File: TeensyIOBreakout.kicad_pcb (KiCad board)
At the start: 2 copper layers, 26 parts, among them J1 Conn_01x02_Male, J10 Conn_01x02_Male, J11 Conn_01x02_Male, J12 Conn_01x02_Male, J13 Conn_01x02_Male, J14 Conn_01x02_Male, J15 Conn_01x02_Male, J16 Conn_01x02_Male, J17 Conn_01x02_Male, J18 Conn_01x02_Male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

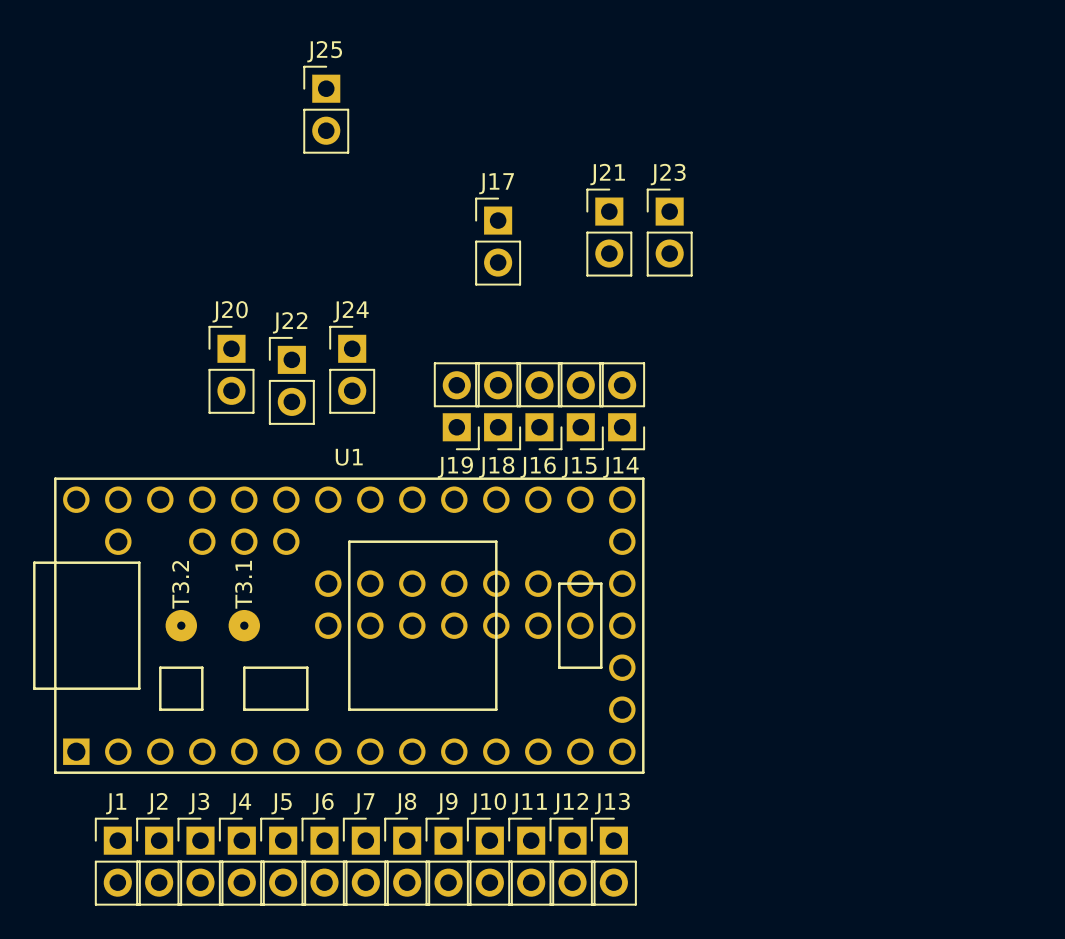
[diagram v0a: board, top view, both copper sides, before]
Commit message: Updated SCH and PCB to use fewer header footprints
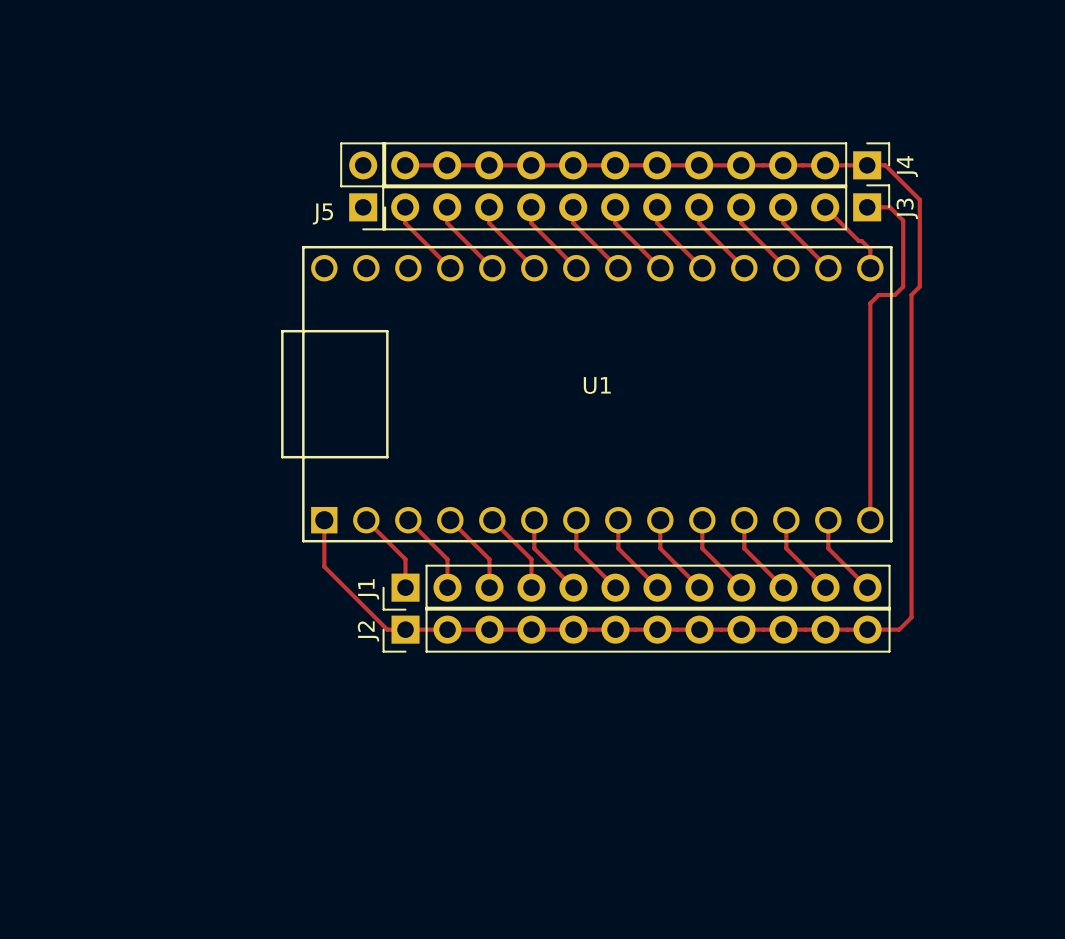
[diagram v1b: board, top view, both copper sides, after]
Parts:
- removed J10, J11, J12, J13, J14, J15, J16, J17, J18, J19, J20, J21, J22, J23, J24, J25, J6, J7, J8, J9: Conn_01x02_Male, Pin_Headers:Pin_Header_Straight_1x02_Pitch2.54mm
- J1, J2, J3, J4: value Conn_01x02_Male -> Conn_01x12_Male; footprint Pin_Headers:Pin_Header_Straight_1x02_Pitch2.54mm -> Pin_Headers:Pin_Header_Straight_1x12_Pitch2.54mm
- U1: footprint teensy:Teensy30_31_32_LC -> Teensy32NoCenterPads:Teensy30_31_32_LC_NoCenterPads
- moved J4 55.7 mm to (146.3, 24.7), turned to 270 degrees
- moved J3 55.6 mm to (146.3, 27.2), turned to 270 degrees
- moved J5 38.6 mm to (115.8, 27.2), turned to 180 degrees
- moved J1 23.2 mm to (118.4, 50.2), turned to 90 degrees
- moved U1 20.5 mm to (130.0, 38.5)
- moved J2 19.6 mm to (118.4, 52.7), turned to 90 degrees
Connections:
- J1 pad 2: GND -> IO_1
- J2 pad 1: IO_1 -> GND
- J3 pad 1: IO_2 -> IO_12
- J3 pad 2: GND -> IO_13
- J4 pad 1: IO_3 -> GND
- J5 pad 1: IO_4 -> Vin
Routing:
- net GND: track 0.00 -> 97.7 mm
- net IO_12: track 0.00 -> 22.0 mm
- net IO_9: track 0.00 -> 5.06 mm
- net IO_8: track 0.00 -> 5.06 mm
- net IO_7: track 0.00 -> 5.06 mm
- net IO_5: track 0.00 -> 5.06 mm
- net IO_4: track 0.00 -> 5.06 mm
- net IO_2: track 0.00 -> 5.06 mm
- net IO_11: track 0.00 -> 5.06 mm
- net IO_10: track 0.00 -> 5.06 mm
- net IO_1: track 0.00 -> 5.06 mm
- net IO_0: track 0.00 -> 5.06 mm
- net IO_3: track 0.00 -> 5.06 mm
- net IO_6: track 0.00 -> 5.06 mm
- net IO_13: track 0.00 -> 4.92 mm
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
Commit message: Added I2C, SPI headers, rear Teensy pins
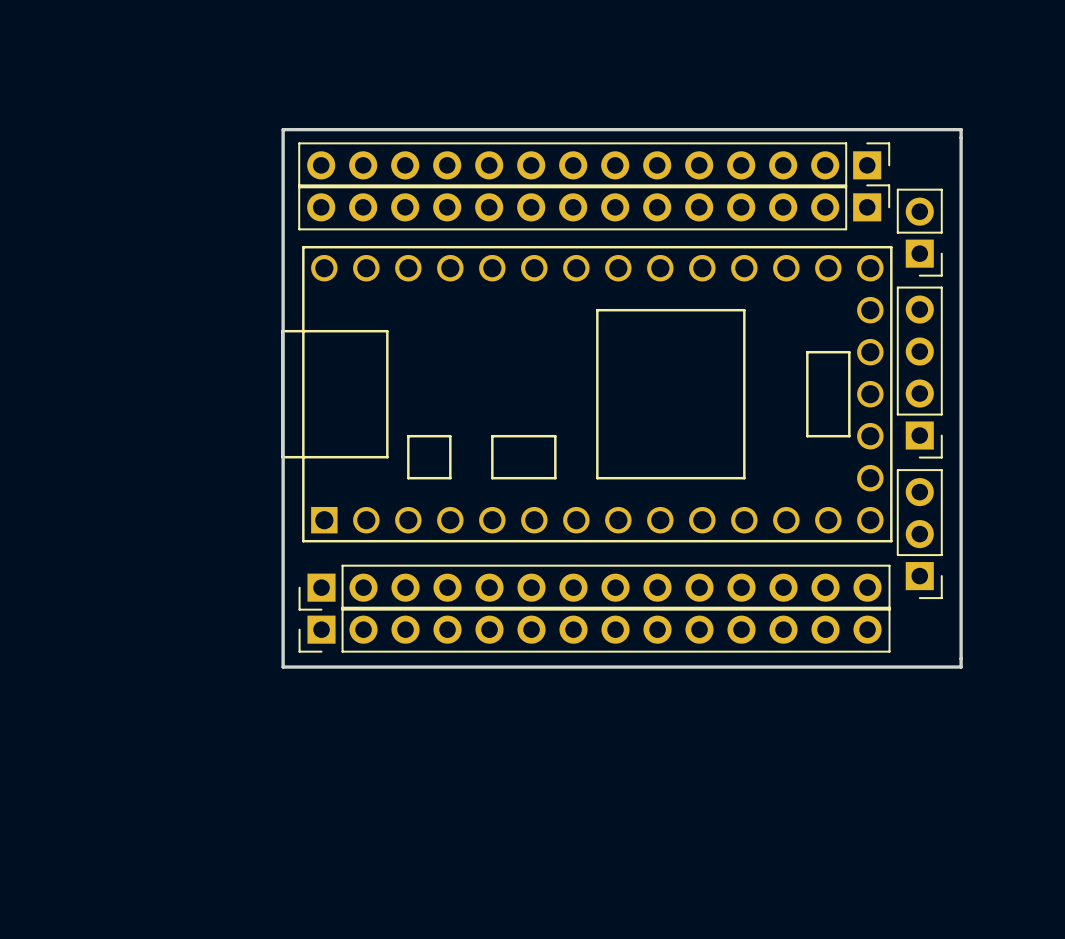
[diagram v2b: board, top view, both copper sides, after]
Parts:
- added G***: LOGO, LOGOS:logo_MLlabs_small, B.Cu at (120.5, 38.5)
- added J6: Conn_01x05_Male, Pin_Headers:Pin_Header_Straight_1x04_Pitch2.54mm, F.Cu at (149.5, 41.0)
- added J7: Conn_01x02_Male, Pin_Headers:Pin_Header_Straight_1x02_Pitch2.54mm, F.Cu at (149.5, 30.0)
- J1, J2, J3, J4: value Conn_01x12_Male -> Conn_01x14_Male; footprint Pin_Headers:Pin_Header_Straight_1x12_Pitch2.54mm -> Pin_Headers:Pin_Header_Straight_1x14_Pitch2.54mm
- J5: value Conn_01x02_Male -> Conn_01x03_Male; footprint Pin_Headers:Pin_Header_Straight_1x02_Pitch2.54mm -> Pin_Headers:Pin_Header_Straight_1x03_Pitch2.54mm
- U1: footprint Teensy32NoCenterPads:Teensy30_31_32_LC_NoCenterPads -> Teensy32NoCenterPads:Teensy30_31_32_LC_EdgePads
- moved J5 40.4 mm to (149.5, 49.5)
- moved J1 5.08 mm to (113.3, 50.2)
- moved J2 5.08 mm to (113.3, 52.7)
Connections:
- J3 pad 1: IO_12 -> PROG
- J3 pad 10: IO_21 -> IO_19
- J3 pad 11: IO_22 -> IO_20
- J3 pad 12: IO_23 -> IO_21
- J3 pad 2: IO_13 -> A14
- J3 pad 3: IO_14 -> IO_12
- J3 pad 4: IO_15 -> IO_13
- J3 pad 5: IO_16 -> IO_14
- J3 pad 6: IO_17 -> IO_15
- J3 pad 7: IO_18 -> IO_16
- J3 pad 8: IO_19 -> IO_17
- J3 pad 9: IO_20 -> IO_18
- J5 pad 1: Vin -> GND
- J5 pad 2: GND -> IO_18
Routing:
- net GND: track 97.7 -> 0.00 mm
- net IO_12: track 22.0 -> 0.00 mm
- net IO_9: track 5.06 -> 0.00 mm
- net IO_8: track 5.06 -> 0.00 mm
- net IO_7: track 5.06 -> 0.00 mm
- net IO_5: track 5.06 -> 0.00 mm
- net IO_4: track 5.06 -> 0.00 mm
- net IO_2: track 5.06 -> 0.00 mm
- net IO_11: track 5.06 -> 0.00 mm
- net IO_10: track 5.06 -> 0.00 mm
- net IO_1: track 5.06 -> 0.00 mm
- net IO_0: track 5.06 -> 0.00 mm
- net IO_3: track 5.06 -> 0.00 mm
- net IO_6: track 5.06 -> 0.00 mm
- net IO_13: track 4.92 -> 0.00 mm
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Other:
- board outline added: 41 x 32.5 mm
- board text added: "Cl.Da.G"
- board text added: "Cl.Di.Do.Cs.G"
- board text added: "IO0 \/ IO11 VBAT 3V3"
- board text added: "IO23 \/ IO12 A14 PROG"
- board text added: "Vin.G"
